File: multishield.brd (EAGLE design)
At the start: 57.6 x 53.7 mm, 21 parts, among them J1 7p-2.54-90d, J2 2x16p-2.54, J3 7p-2.54-90d, J4 2x6p-2.54, J5 7p-2.54-90d, J6 7p-2.54-90d, K2 TS-1101F, M1 ARDUINO_R3_ICSP, SW1 SK-12D01, U1 AD595AQ-DIP14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

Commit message: various improvements and addition of LED at D9
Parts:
- added D9: SR302DC, Seeed-OPL-Diode:LED2-2.54-D3.0MM
- added R2: 150Ω, Seeed-OPL-Resistor:PR-D2.3XL6.5MM
- moved J5 0.80 mm to (4.57, 40.5)
- moved J6 0.70 mm to (4.57, 22.4)
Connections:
- net N$18 renamed D9A
- removed net N$34: J2.23, J5.1, U2.15
- new net D9B: D9.A, J2.23, J5.1, U2.15
- new net N$18: D9.K, R2.1
- net GND: now also R2.2
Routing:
- net D9B: track 0.00 -> 76.1 mm, vias 0 -> 1
- net N$34: track 41.9 -> 0.00 mm, vias 1 -> 0
- net N$18: track 0.00 -> 8.53 mm
- net SCK: track 63.6 -> 64.7 mm
- net VCC: track 93.3 -> 92.6 mm
- net MISO: track 82.4 -> 83.0 mm
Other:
- board size 57.6 x 53.7 mm -> 57.6 x 53.6 mm
- board text added: "OPR"
- board text removed: "OP"

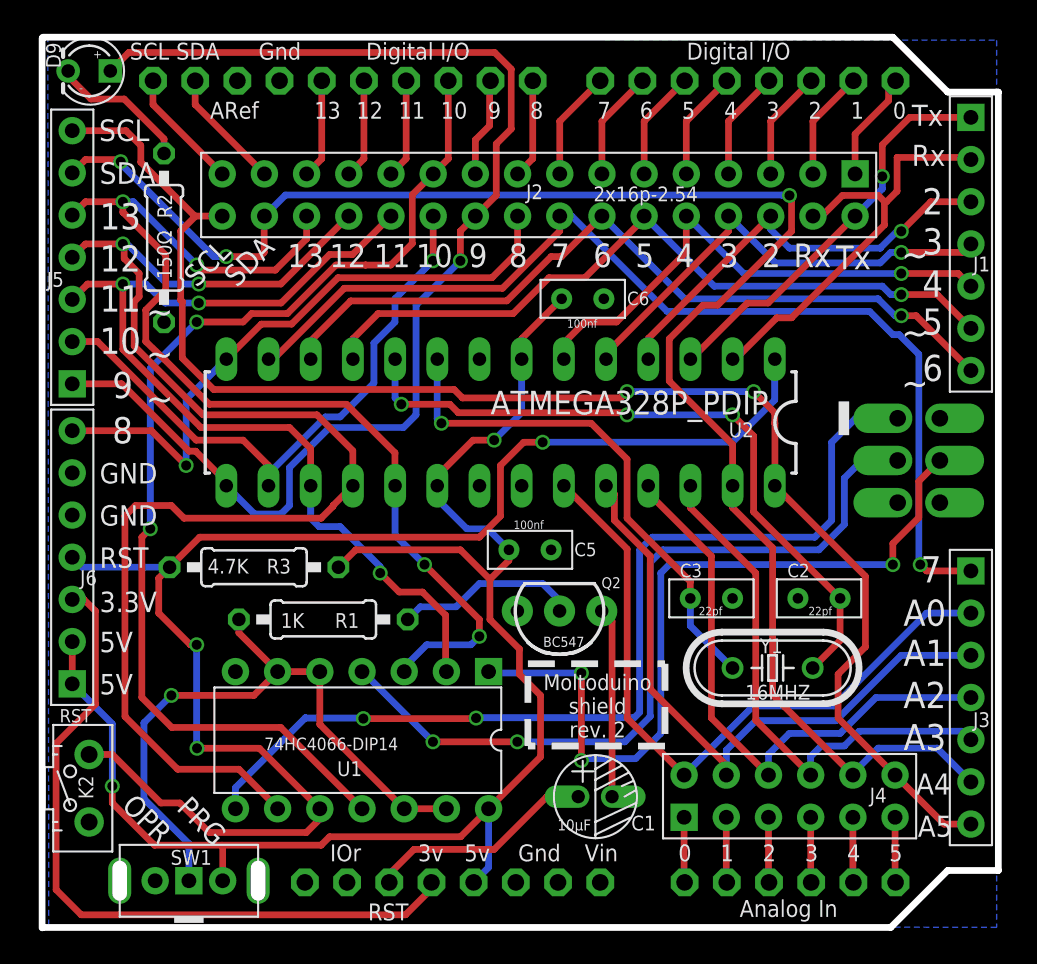
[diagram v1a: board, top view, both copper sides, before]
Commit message: changed 0 and 1 labels to rx and tx
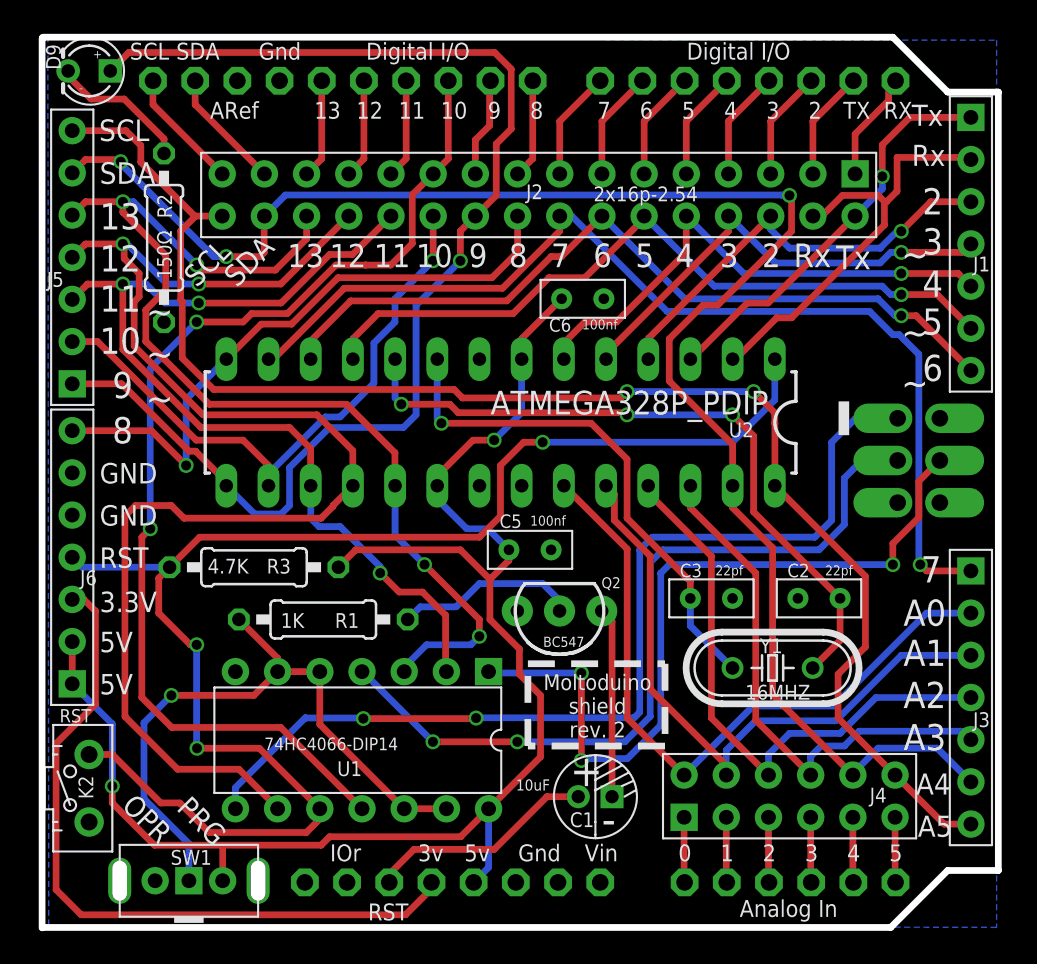
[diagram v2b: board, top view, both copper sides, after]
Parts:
- C1: value 10µF -> 10uF
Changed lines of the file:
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@@
 <attribute name="VALUE" x="6.223" y="10.668" size="0.6096" layer="27" ratio="11" rot="R270"/>
 </element>
-<element name="C1" library="Seeed-OPL-Capacitor" package="PC-D5.0MM" value="10µF" x="36.068" y="8.001" smashed="yes">
+<element name="C1" library="Seeed-OPL-Capacitor" package="PC-D5.0MM" value="10uF" x="36.068" y="8.001" smashed="yes">
 <attribute name="MPN" value="100µF/16V  5X7" x="36.068" y="8.001" size="1.25" layer="27" font="vector" display="off"/>
-<attribute name="NAME" x="38.227" y="5.969" size="0.889" layer="25" ratio="11"/>
-<attribute name="VALUE" x="33.782" y="5.969" size="0.6604" layer="25" ratio="10"/>
+<attribute name="NAME" x="34.527" y="6.169" size="0.889" layer="25" ratio="11"/>
+<attribute name="VALUE" x="31.282" y="8.369" size="0.67" layer="25" ratio="10"/>
 </element>
 <element name="R1" library="Seeed-OPL-Resistor" package="PR-D2.3XL6.5MM" value="1K" x="19.812" y="18.669" smashed="yes" rot="R180">
@@
 <attribute name="MPN" value="CS1-D5Y5V2A104ZSP" x="49.53" y="19.939" size="1.228" layer="27" display="off"/>
 <attribute name="NAME" x="47.625" y="21.209" size="0.8128" layer="25" ratio="10"/>
-<attribute name="VALUE" x="48.895" y="18.923" size="0.508" layer="25" ratio="10"/>
+<attribute name="VALUE" x="49.895" y="21.323" size="0.6" layer="25" ratio="10"/>
 <attribute name="NAME" x="48.514" y="19.685" size="0.4064" layer="33" ratio="10"/>
 </element>
@@
 <attribute name="MPN" value="CS1-D5Y5V2A104ZSP" x="43.053" y="19.939" size="1.228" layer="27" display="off"/>
 <attribute name="NAME" x="41.148" y="21.209" size="0.8128" layer="25" ratio="10"/>
-<attribute name="VALUE" x="42.291" y="18.923" size="0.508" layer="25" ratio="10"/>
+<attribute name="VALUE" x="43.291" y="21.323" size="0.6" layer="25" ratio="10"/>
 <attribute name="NAME" x="42.037" y="19.685" size="0.4064" layer="33" ratio="10"/>
 </element>
@@
 <element name="C5" library="Seeed-OPL-Capacitor" package="CERAMIC-2.54" value="100nf" x="32.131" y="22.86" smashed="yes">
 <attribute name="MPN" value="CC1-F5SL2A101KSPW" x="32.131" y="22.86" size="1.778" layer="27" display="off"/>
-<attribute name="NAME" x="34.798" y="22.479" size="0.8128" layer="25" ratio="10"/>
-<attribute name="VALUE" x="31.142" y="24.117" size="0.508" layer="25" ratio="10"/>
+<attribute name="NAME" x="30.298" y="24.179" size="0.8128" layer="25" ratio="10"/>
+<attribute name="VALUE" x="32.142" y="24.317" size="0.6" layer="25" ratio="10"/>
 <attribute name="NAME" x="31.115" y="22.606" size="0.4064" layer="33" ratio="10"/>
 </element>
 <element name="C6" library="Seeed-OPL-Capacitor" package="CERAMIC-2.54" value="100nf" x="35.306" y="37.973" smashed="yes">
 <attribute name="MPN" value="CC1-F5SL2A101KSPW" x="35.306" y="37.973" size="1.778" layer="27" display="off"/>
-<attribute name="NAME" x="37.973" y="37.592" size="0.8128" layer="25" ratio="10"/>
-<attribute name="VALUE" x="34.363" y="36.23" size="0.508" layer="25" ratio="10"/>
+<attribute name="NAME" x="33.273" y="35.992" size="0.8128" layer="25" ratio="10"/>
+<attribute name="VALUE" x="35.263" y="36.13" size="0.6" layer="25" ratio="10"/>
 <attribute name="NAME" x="34.29" y="37.719" size="0.4064" layer="33" ratio="10"/>
 </element>
@@
 <element name="D9" library="Seeed-OPL-Diode" package="LED2-2.54-D3.0MM" value="SR302DC" x="5.596" y="51.689" smashed="yes" rot="R180">
 <attribute name="MPN" value="SR302DC" x="5.596" y="51.689" size="1.778" layer="27" rot="R180" display="off"/>
-<attribute name="NAME" x="2.997" y="53.401" size="0.889" layer="25" ratio="11" rot="R270"/>
+<attribute name="NAME" x="2.997" y="53.301" size="0.889" layer="25" ratio="11" rot="R270"/>
 </element>
 <element name="R2" library="Seeed-OPL-Resistor" package="PR-D2.3XL6.5MM" value="150Ω" x="10.098" y="41.771" smashed="yes" rot="R270">
@@
 <wire x1="29.7215" y1="15.444" x2="29.638" y2="15.5275" width="0.4064" layer="16"/>
 <wire x1="35.224" y1="10.179" x2="35.332" y2="10.287" width="0.4064" layer="16"/>
-<wire x1="35.332" y1="10.287" x2="38.481" y2="10.287" width="0.4064" layer="16"/>
-<wire x1="38.481" y1="10.287" x2="40.005" y2="11.811" width="0.4064" layer="16"/>
-<wire x1="40.005" y1="11.811" x2="40.005" y2="21.463" width="0.4064" layer="16"/>
 <via x="53.975" y="21.971" extent="1-16" drill="0.6" shape="square"/>
 <wire x1="53.975" y1="21.971" x2="53.975" y2="23.241" width="0.4064" layer="1"/>
@@
 <wire x1="55.5371" y1="26.9875" x2="56.7896" y2="28.24" width="0.4064" layer="1"/>
 <wire x1="56.7896" y1="28.24" x2="56.805" y2="28.24" width="0.4064" layer="1"/>
-<wire x1="40.005" y1="21.463" x2="40.513" y2="21.971" width="0.4064" layer="16"/>
+<wire x1="40" y1="21.458" x2="40.513" y2="21.971" width="0.4064" layer="16"/>
 <wire x1="40.513" y1="21.971" x2="53.975" y2="21.971" width="0.4064" layer="16"/>
+<wire x1="35.332" y1="10.287" x2="37.987" y2="10.287" width="0.4064" layer="16"/>
+<wire x1="37.987" y1="10.287" x2="40" y2="12.3" width="0.4064" layer="16"/>
+<wire x1="40" y1="12.3" x2="40" y2="21.458" width="0.4064" layer="16"/>
 </signal>
 <signal name="N$40">
@@
 <wire x1="8.89" y1="7.874" x2="8.89" y2="12.446" width="0.4064" layer="16"/>
 <contactref element="R1" pad="2"/>
-<wire x1="16.938" y1="15.5275" x2="14.605" y2="17.8605" width="0.4064" layer="1"/>
-<wire x1="14.605" y1="17.8605" x2="14.605" y2="18.669" width="0.4064" layer="1"/>
 <wire x1="19.478" y1="12.3525" x2="24.558" y2="7.2725" width="0.4064" layer="1"/>
 <wire x1="19.478" y1="15.5275" x2="19.478" y2="12.3525" width="0.4064" layer="1"/>
+<wire x1="16.938" y1="15.5275" x2="16.938" y2="16.336" width="0.4064" layer="1"/>
+<wire x1="16.938" y1="16.336" x2="14.605" y2="18.669" width="0.4064" layer="1"/>
 </signal>
 <signal name="SCK">

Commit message: no more short circuiting while switch in the middle position
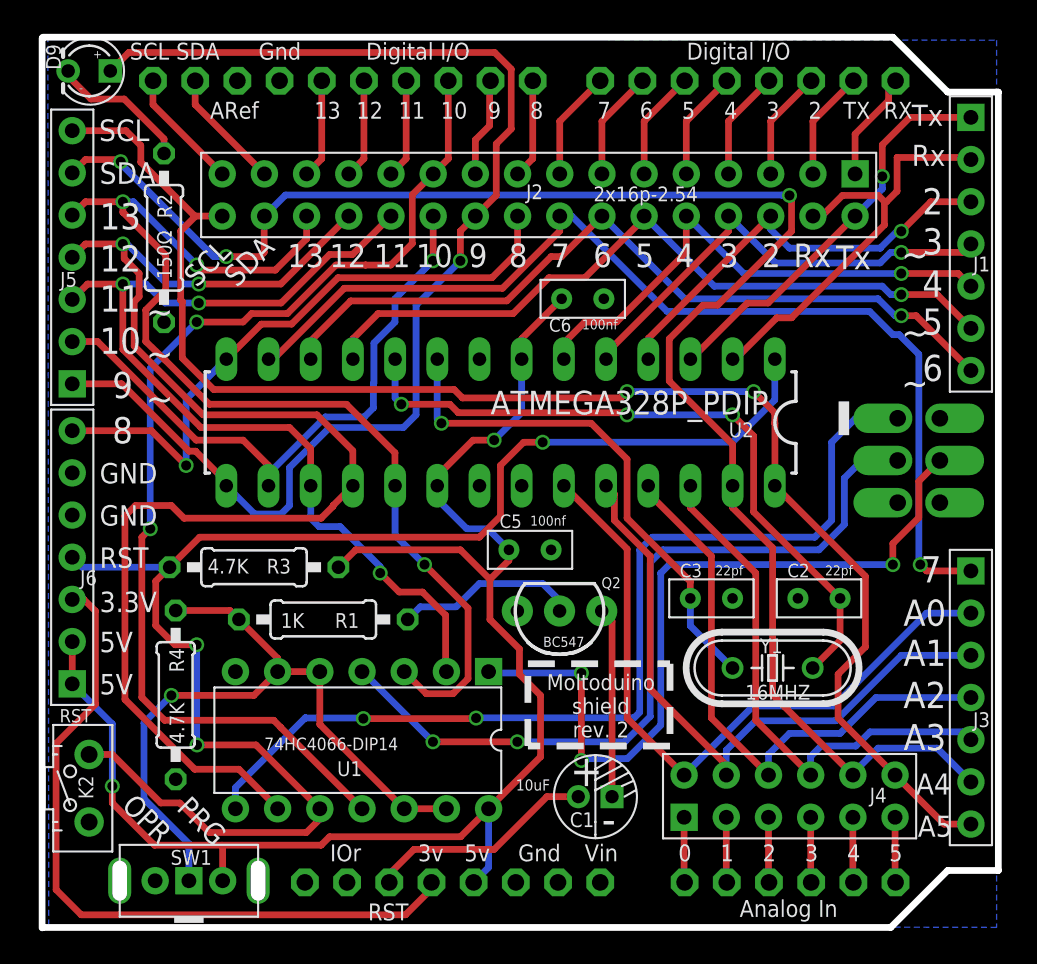
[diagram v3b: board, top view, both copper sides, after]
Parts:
- added R4: 4.7K, Seeed-OPL-Resistor:PR-D2.3XL6.5MM
- moved U$4 0.60 mm to (10.2, 6.13)
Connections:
- net GND: now also R4.1; no longer SW1.B
- net N$56: now also R4.2
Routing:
- net N$56: track 39.5 -> 43.5 mm
- net SCK: track 64.7 -> 66.2 mm, vias 4 -> 3
- net N$35: track 37.0 -> 37.8 mm
- net MISO: track 83.0 -> 82.4 mm
- net SLAVE-RESET: track 89.0 -> 89.6 mm
